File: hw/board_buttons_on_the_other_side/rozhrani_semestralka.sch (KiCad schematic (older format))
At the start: 58 parts, among them P1 DISPLAY_CONN, P2 DISPLAY_VCC_CON, P3 USB_B, U1 MCP2210, U2 MIC5504-3.3, U3 Joystick, U4 LM239, U5 CD4532, U6 NPIC6C596, U7 NE555, U8 PB6149L, U9 PB6149L

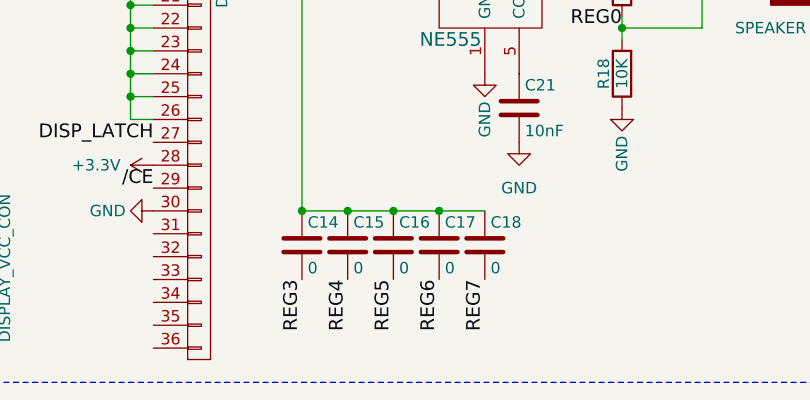
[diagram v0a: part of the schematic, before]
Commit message: created version 1.1.0 -- usb connector rotated -- there is no compatible with printed casing, please use version 1.0.0B
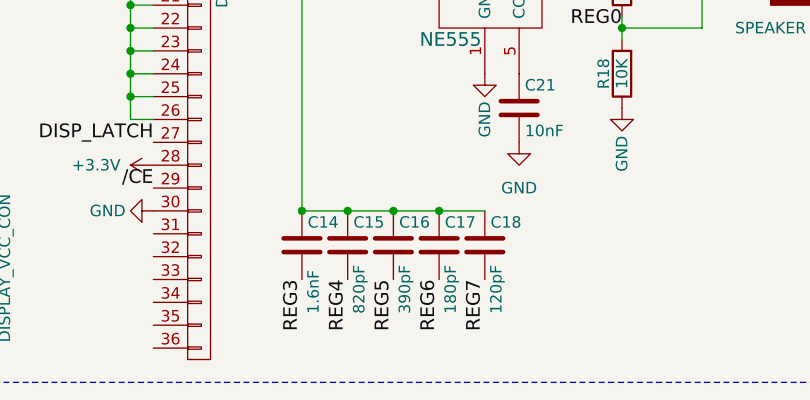
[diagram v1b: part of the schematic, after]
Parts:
- C14: value 0 -> 1.6nF
- C15: value 0 -> 820pF
- C16: value 0 -> 390pF
- C17: value 0 -> 180pF
- C18: value 0 -> 120pF
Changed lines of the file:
@@
 P 3250 7050
 F 0 "C15" H 3275 7150 50  0000 L CNN
-F 1 "0" H 3275 6950 50  0000 L CNN
+F 1 "820pF" V 3300 6750 50  0000 L CNN
 F 2 "Capacitors_SMD:C_0603_HandSoldering" H 3288 6900 30  0001 C CNN
 F 3 "" H 3250 7050 60  0000 C CNN
@@
 P 3450 7050
 F 0 "C16" H 3475 7150 50  0000 L CNN
-F 1 "0" H 3475 6950 50  0000 L CNN
+F 1 "390pF" V 3500 6750 50  0000 L CNN
 F 2 "Capacitors_SMD:C_0603_HandSoldering" H 3488 6900 30  0001 C CNN
 F 3 "" H 3450 7050 60  0000 C CNN
@@
 P 3650 7050
 F 0 "C17" H 3675 7150 50  0000 L CNN
-F 1 "0" H 3675 6950 50  0000 L CNN
+F 1 "180pF" V 3700 6750 50  0000 L CNN
 F 2 "Capacitors_SMD:C_0603_HandSoldering" H 3688 6900 30  0001 C CNN
 F 3 "" H 3650 7050 60  0000 C CNN
@@
 P 3850 7050
 F 0 "C18" H 3875 7150 50  0000 L CNN
-F 1 "0" H 3875 6950 50  0000 L CNN
+F 1 "120pF" V 3900 6750 50  0000 L CNN
 F 2 "Capacitors_SMD:C_0603_HandSoldering" H 3888 6900 30  0001 C CNN
 F 3 "" H 3850 7050 60  0000 C CNN
@@
 P 3050 7050
 F 0 "C14" H 3075 7150 50  0000 L CNN
-F 1 "0" H 3075 6950 50  0000 L CNN
+F 1 "1.6nF" V 3100 6750 50  0000 L CNN
 F 2 "Capacitors_SMD:C_0603_HandSoldering" H 3088 6900 30  0001 C CNN
 F 3 "" H 3050 7050 60  0000 C CNN

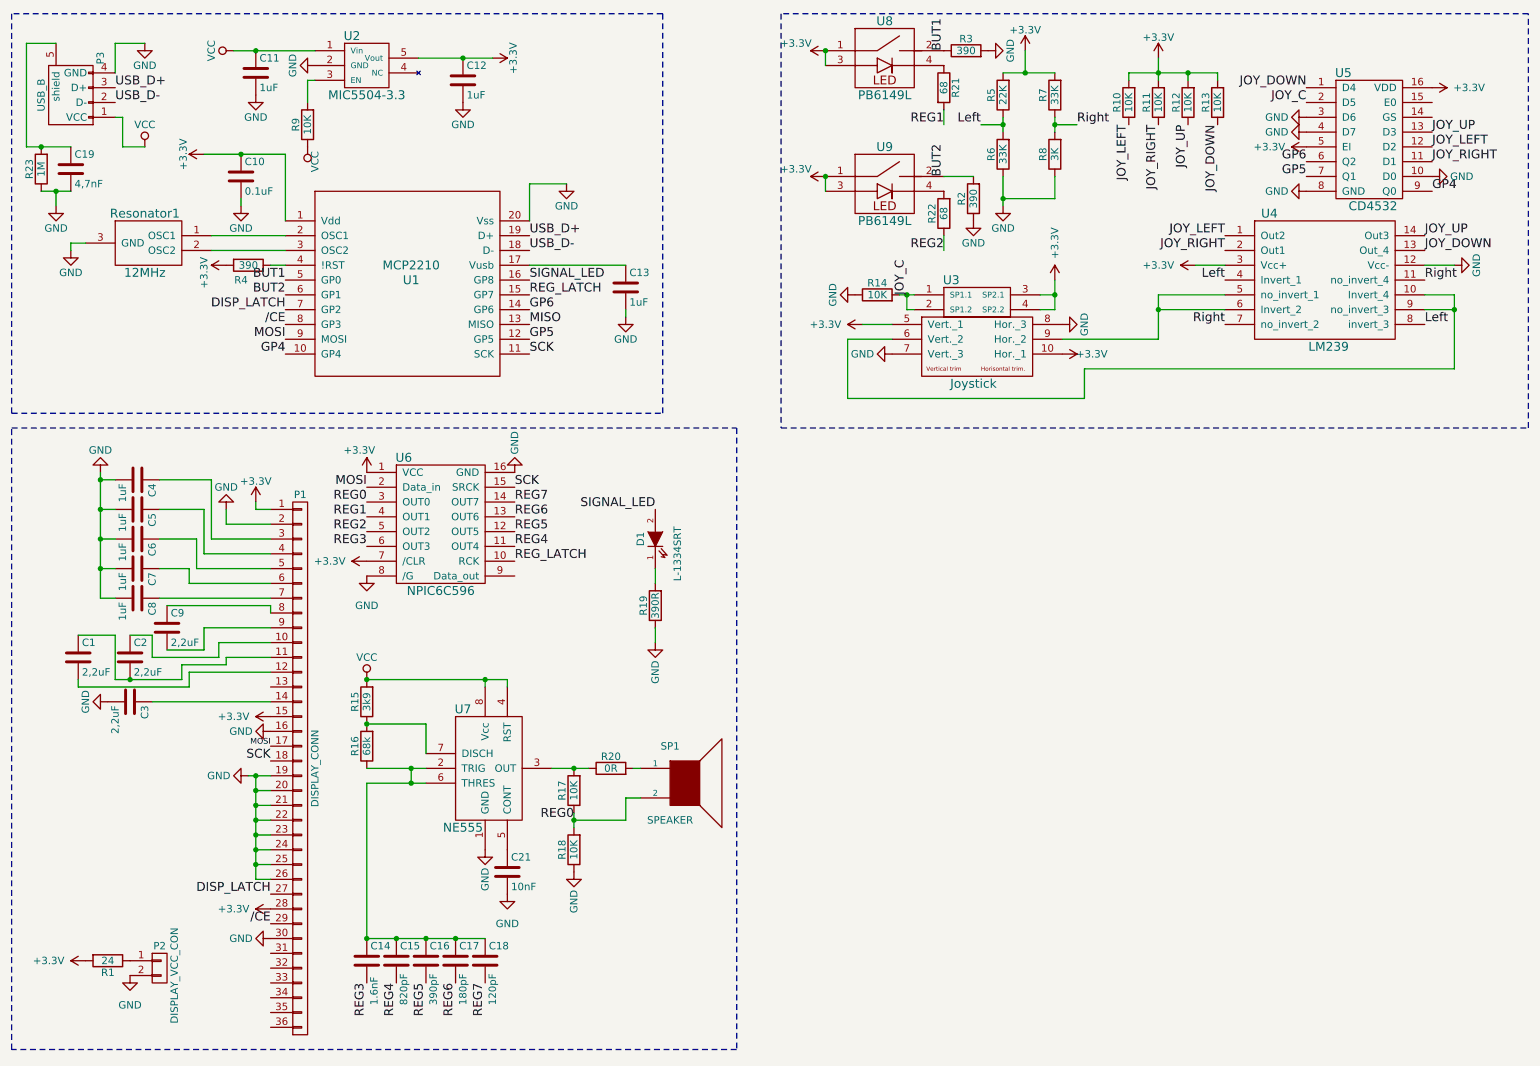
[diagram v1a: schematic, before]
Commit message: Eddited board to version 1.1.1 - now one of button has choise for 2 colour also added values to silk screen
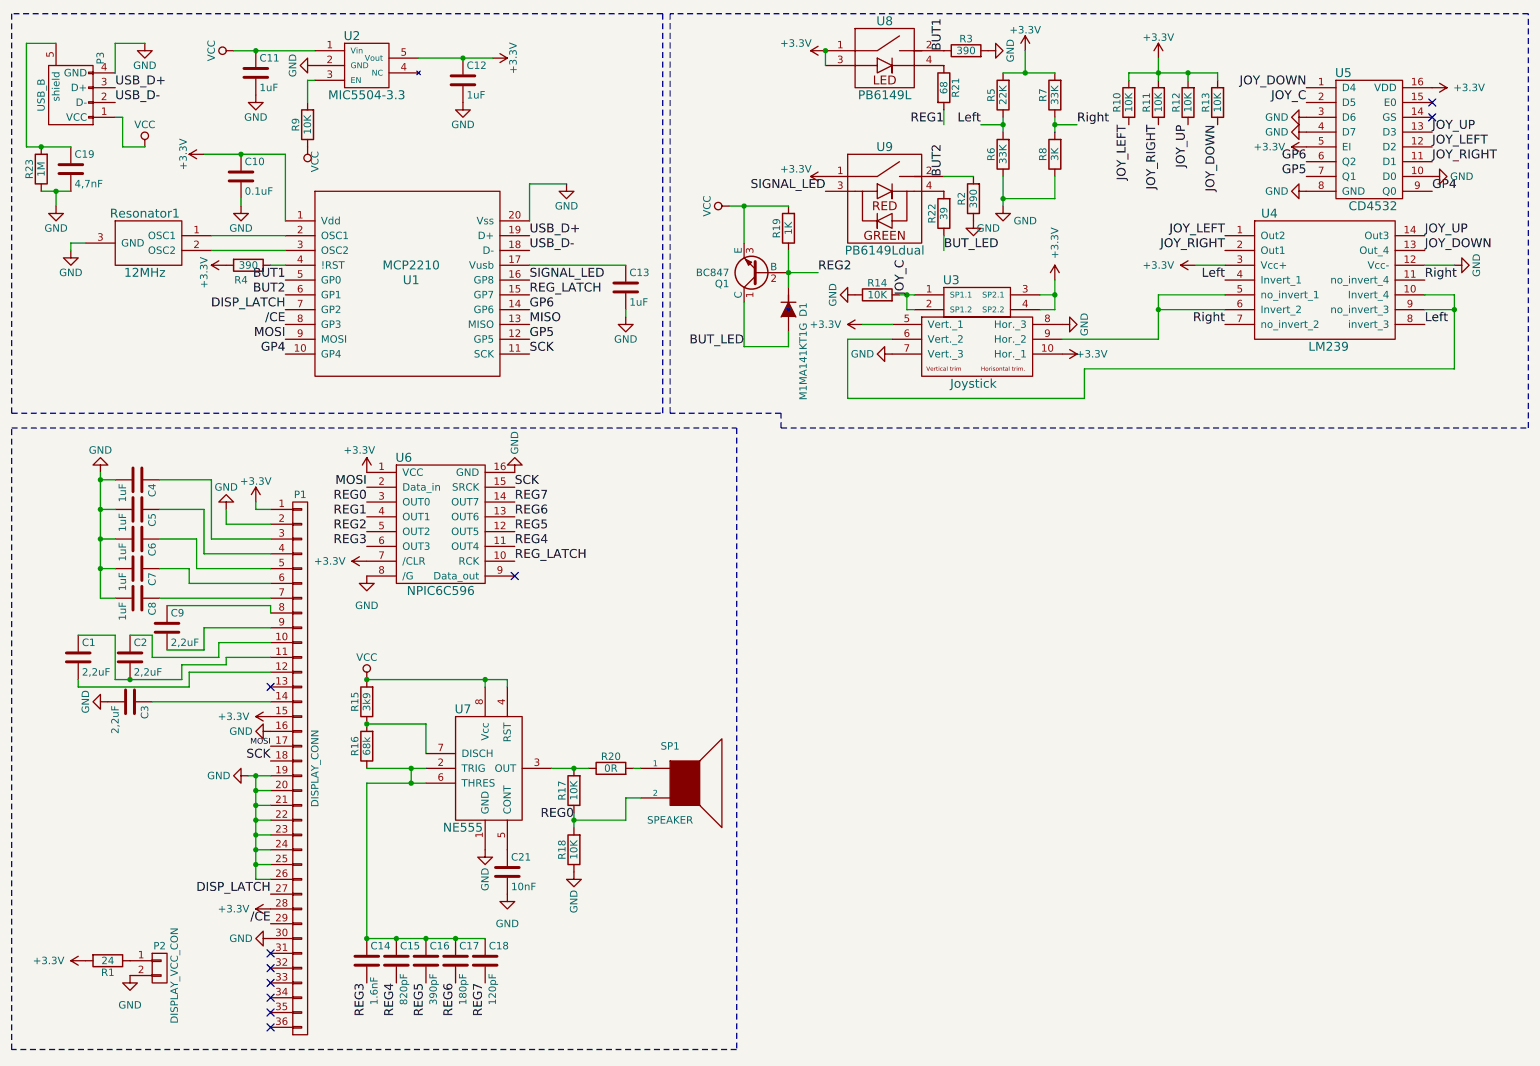
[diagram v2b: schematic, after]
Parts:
- removed D1: L-1334SRT, LEDs:LED-3MM, symbol LED
- removed U9: PB6149L, pcb:PB6149L, symbol PB6149L
- added D1: M1MA141KT1G, TO_SOT_Packages_SMD:SOT-323, symbol M1MA141KT1G
- added Q1: BC847, TO_SOT_Packages_SMD:SOT-323, symbol BC547
- added U9: PB6149Ldual, pcb:PB6149L, symbol PB6149Ldual
- R19: value 390R -> 1K
- R22: value 68 -> 39
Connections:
- net +3V3: now also U9.1
- net BUT2: now also U9.2
- net GND: no longer R19.1
- net REG2: now also R19.1, D1.3 (K), Q1.2 (B); no longer R22.1
- net SIGNAL_LED: now also U9.3
- net VCC: now also R19.2, Q1.3 (E)
- net at R22.2: now also U9.4
- new net BUT_LED: D1.1 (A), Q1.1 (C), R22.1
- no-connect marks 0 -> 10
